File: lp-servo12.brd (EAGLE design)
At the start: 76.1 x 43.2 mm, 63 parts, among them U1 TPS54526PWP, U2 LMV358

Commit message: Added copyright and license text to board and schematic. Cosmetic changes only, no electrical or layout changes. Cleaned up schematic, added some comments. Change LICENSE to use creative commons attribution. Reflowed text in the README.
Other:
- board text added: "Copyright (c) 2013 by Joe Kroesche (kroesche.org) All rights reserved."
- board text added: "This work is licensed under the Creative Commons Attribution 3.0 Unported License. To view a copy of this license, visit http://creativecommons.org/licenses/by/3.0/."
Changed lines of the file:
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@@
 <text x="50.8" y="12.7" size="1.27" layer="22" font="vector" rot="MR0" align="top-left">LAUNCHPAD SUPPLY (5V)</text>
 <text x="53.34" y="10.16" size="1.27" layer="22" font="vector" rot="MR0" align="top-left">6. SxA/B &lt;-&gt; WIDE TIMER xA/B</text>
+<text x="0" y="-7.62" size="1.27" layer="51" font="vector">Copyright (c) 2013 by Joe Kroesche (kroesche.org)
+All rights reserved.</text>
+<text x="0" y="-17.78" size="1.27" layer="51" font="vector">This work is licensed under the
+Creative Commons Attribution 3.0 Unported License.
+To view a copy of this license, visit
+http://creativecommons.org/licenses/by/3.0/.</text>
 </plain>
 <attributes>
@@
 </board>
 </drawing>
+<compatibility>
+<note version="6.3" minversion="6.2.2" severity="warning">
+Since Version 6.2.2 text objects can contain more than one line,
+which will not be processed correctly with this version.
+</note>
+</compatibility>
 </eagle>

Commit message: Fixed some resistor values on the voltage measuring op-amp circuit. The orginal values were not correct for a 2S battery (they were for a 1S battery). Updated the bom files to reflect the changes in the resistor values. Net effect is that two 22K resistors go away and 2 30K are added, some ref designators change.
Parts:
- R16: value 22K -> 30K
- R18: value 10K -> 30K
- R19: value 22K -> 10K
- R20: value 10K -> 15K
- R21: value 15K -> 10K
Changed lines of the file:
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@@
 <attribute name="PARTNO" value="LMV358QDR" x="38.1" y="7.62" size="1.778" layer="27" rot="R90" display="off"/>
 </element>
-<element name="R16" library="SparkFun-Resistors" package="0805" value="22K" x="32.385" y="6.35" smashed="yes" rot="R270">
+<element name="R16" library="SparkFun-Resistors" package="0805" value="30K" x="32.385" y="6.35" smashed="yes" rot="R270">
 <attribute name="NAME" x="31.75" y="4.0005" size="0.8128" layer="25"/>
 <attribute name="VALUE" x="30.988" y="7.366" size="0.4064" layer="27" rot="R270"/>
@@
 <attribute name="VOLT" value="20V" x="32.385" y="6.35" size="1.778" layer="27" rot="R270" display="off"/>
 <attribute name="SIZE" value="(0805)" x="32.385" y="6.35" size="1.778" layer="27" rot="R270" display="off"/>
-<attribute name="PARTNO" value="RES_22K_20V_1PCT_0805" x="32.385" y="6.35" size="1.778" layer="27" rot="R270" display="off"/>
+<attribute name="PARTNO" value="RES_30K_20V_1PCT_0805" x="32.385" y="6.35" size="1.778" layer="27" rot="R270" display="off"/>
 </element>
 <element name="R17" library="SparkFun-Resistors" package="0805" value="10K" x="32.385" y="9.525" smashed="yes" rot="R270">
@@
 <attribute name="PARTNO" value="RES_10K_20V_1PCT_0805" x="32.385" y="9.525" size="1.778" layer="27" rot="R270" display="off"/>
 </element>
-<element name="R18" library="SparkFun-Resistors" package="0805" value="10K" x="34.29" y="12.065" smashed="yes">
+<element name="R18" library="SparkFun-Resistors" package="0805" value="30K" x="34.29" y="12.065" smashed="yes">
 <attribute name="NAME" x="33.782" y="13.1445" size="0.8128" layer="25"/>
 <attribute name="VALUE" x="33.274" y="10.668" size="0.4064" layer="27"/>
@@
 <attribute name="VOLT" value="20V" x="34.29" y="12.065" size="1.778" layer="27" display="off"/>
 <attribute name="SIZE" value="(0805)" x="34.29" y="12.065" size="1.778" layer="27" display="off"/>
-<attribute name="PARTNO" value="RES_10K_20V_1PCT_0805" x="34.29" y="12.065" size="1.778" layer="27" display="off"/>
+<attribute name="PARTNO" value="RES_30K_20V_1PCT_0805" x="34.29" y="12.065" size="1.778" layer="27" display="off"/>
 </element>
-<element name="R19" library="SparkFun-Resistors" package="0805" value="22K" x="38.1" y="12.065" smashed="yes" rot="R180">
+<element name="R19" library="SparkFun-Resistors" package="0805" value="10K" x="38.1" y="12.065" smashed="yes" rot="R180">
 <attribute name="NAME" x="39.37" y="13.7795" size="0.8128" layer="25" rot="R180"/>
 <attribute name="VALUE" x="39.116" y="13.462" size="0.4064" layer="27" rot="R180"/>
@@
 <attribute name="VOLT" value="20V" x="38.1" y="12.065" size="1.778" layer="27" rot="R180" display="off"/>
 <attribute name="SIZE" value="(0805)" x="38.1" y="12.065" size="1.778" layer="27" rot="R180" display="off"/>
-<attribute name="PARTNO" value="RES_22K_20V_1PCT_0805" x="38.1" y="12.065" size="1.778" layer="27" rot="R180" display="off"/>
+<attribute name="PARTNO" value="RES_10K_20V_1PCT_0805" x="38.1" y="12.065" size="1.778" layer="27" rot="R180" display="off"/>
 </element>
-<element name="R20" library="SparkFun-Resistors" package="0805" value="10K" x="43.815" y="5.715" smashed="yes" rot="R270">
+<element name="R20" library="SparkFun-Resistors" package="0805" value="15K" x="43.815" y="5.715" smashed="yes" rot="R270">
 <attribute name="NAME" x="45.085" y="5.2705" size="0.8128" layer="25"/>
 <attribute name="VALUE" x="42.418" y="6.731" size="0.4064" layer="27" rot="R270"/>
@@
 <attribute name="VOLT" value="20V" x="43.815" y="5.715" size="1.778" layer="27" rot="R270" display="off"/>
 <attribute name="SIZE" value="(0805)" x="43.815" y="5.715" size="1.778" layer="27" rot="R270" display="off"/>
-<attribute name="PARTNO" value="RES_10K_20V_1PCT_0805" x="43.815" y="5.715" size="1.778" layer="27" rot="R270" display="off"/>
+<attribute name="PARTNO" value="RES_15K_20V_1PCT_0805" x="43.815" y="5.715" size="1.778" layer="27" rot="R270" display="off"/>
 </element>
-<element name="R21" library="SparkFun-Resistors" package="0805" value="15K" x="43.815" y="9.525" smashed="yes" rot="R270">
+<element name="R21" library="SparkFun-Resistors" package="0805" value="10K" x="43.815" y="9.525" smashed="yes" rot="R270">
 <attribute name="NAME" x="45.085" y="9.3345" size="0.8128" layer="25"/>
 <attribute name="VALUE" x="42.418" y="10.541" size="0.4064" layer="27" rot="R270"/>
@@
 <attribute name="VOLT" value="20V" x="43.815" y="9.525" size="1.778" layer="27" rot="R270" display="off"/>
 <attribute name="SIZE" value="(0805)" x="43.815" y="9.525" size="1.778" layer="27" rot="R270" display="off"/>
-<attribute name="PARTNO" value="RES_15K_20V_1PCT_0805" x="43.815" y="9.525" size="1.778" layer="27" rot="R270" display="off"/>
+<attribute name="PARTNO" value="RES_10K_20V_1PCT_0805" x="43.815" y="9.525" size="1.778" layer="27" rot="R270" display="off"/>
 </element>
 <element name="C13" library="SparkFun-Passives" package="0805" value="1uF" x="36.195" y="3.175" smashed="yes">

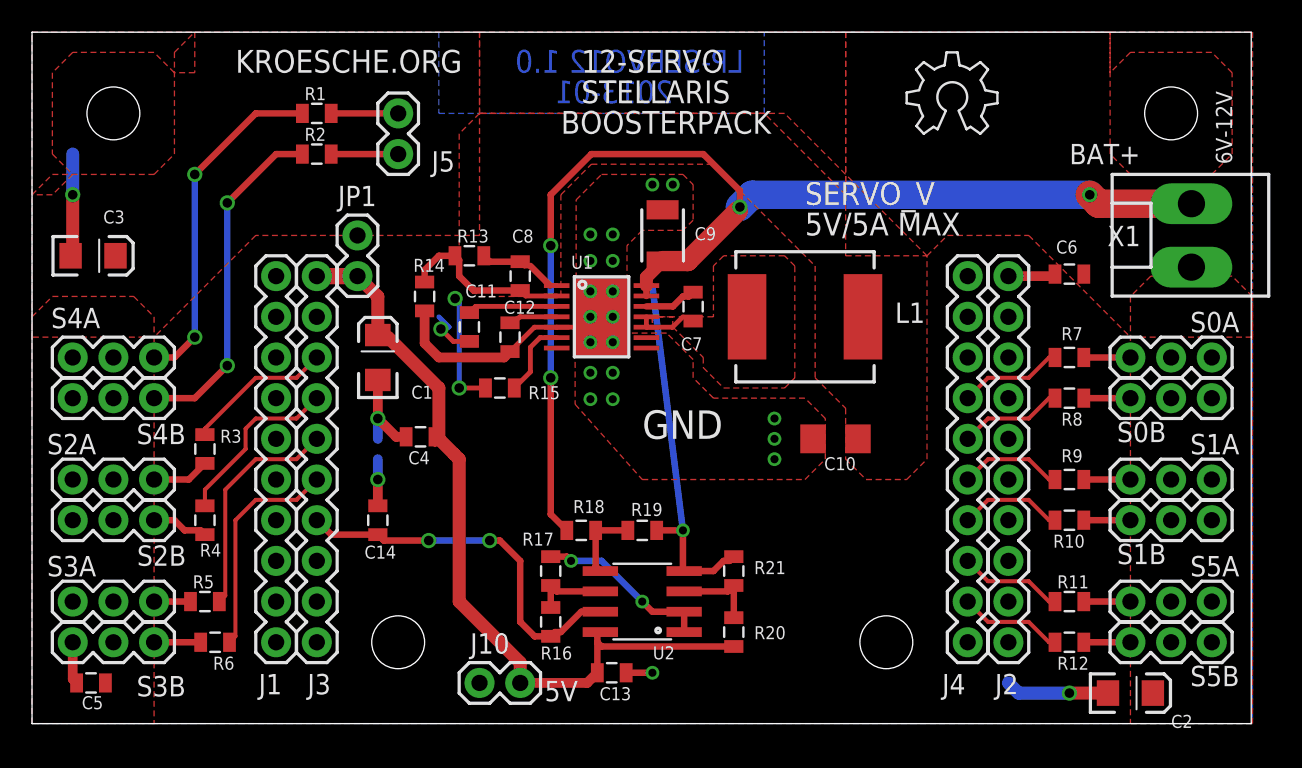
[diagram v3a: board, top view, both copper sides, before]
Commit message: Fixed missing pullup on enable line and unconnectd trace on feeback signal for power supply.  Those were the two known bugs. Also moved one of the moounting holes and moved the power connector around so that it would not overhang the edge of the board, and also changed the orientation to come out the top instead of the side.
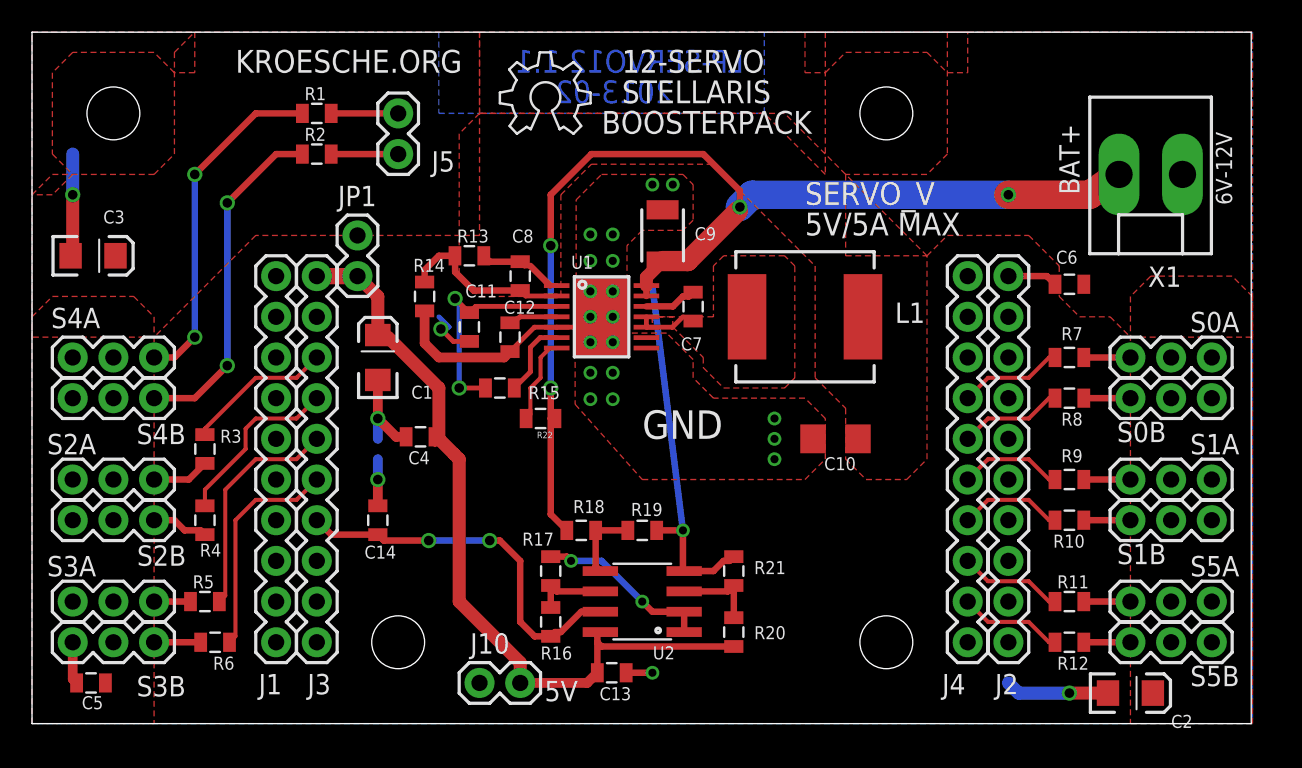
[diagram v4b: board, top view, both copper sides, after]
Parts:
- added R22: 100K, SparkFun-Resistors:0805
- moved LOGO2 25.4 mm to (29.2, 36.8)
- moved STANDOFF4 17.8 mm to (53.3, 38.1)
- moved X1 4.58 mm to (69.8, 34.3), turned to 180 degrees
- moved C6 0.64 mm to (64.8, 27.4)
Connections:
- removed net +3V3: J1.1
- new net N$19: R22.2, U1.7
- net VBAT: now also R22.1
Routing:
- net N$19: track 0.00 -> 5.44 mm
- net VBAT: track 73.5 -> 69.7 mm
- net N$22: track 12.9 -> 14.2 mm
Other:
- board text added: "2013-02"
- board text added: "LP-SERVO12 1.1"
- board text removed: "2013-01"
- board text removed: "LP-SERVO12 1.0"
